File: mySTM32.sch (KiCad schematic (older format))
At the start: 114 parts, among them J1 conn1X2, J10 DB9_Female****, J11 USB_OTG, J12 conn2X16, J13 conn2X3, J14 Conn_02x02, J15 conn2X3, J16 conn1X2, J17 conn2X2, J18 JTAG, J19 Conn_02x17_Odd_Even, J2 USB_OTG, J20 Conn_02x22_Odd_Even, J21 conn2X9, J22 conn2X3, J23 Conn2x4, J3 conn2X3, J4 conn2X2, J5 conn2X2, J6 conn1X2, J7 Conn_01x02, J8 Conn2x4, J9 conn2X4, Q1 Q_NPN_BEC(S8050), Q2 Q_NPN_BEC, Q3 Q_NPN_BEC(S8050), SW1 KFT8.0, SW2 WAKUP, SW3 RESET, SW4 KE1, SW5 KEY2, U1 AT24C02, U2 W25Q16, U3 SD-Card, U4 SP3485, U5 SN65HVD230, U6 CH340G, U7 AMS1117, U8 SP3232, U9 STM32F103VET6, Y1 12MHz, Y2 32.768KHz, Y3 8MHz

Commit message: [power]
Signed-off-by: EasonLiang <liangyx25@163.com>
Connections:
- net +5V: no longer J15.2 (Pin_2), J15.4 (Pin_4), J15.6 (Pin_6)
- net 5V: now reaches C7.1, C9.1, SW1.2, SW1.5, U7.3 (VIN)
- net 5V: now also J15.2 (Pin_2), J15.4 (Pin_4), J15.6 (Pin_6)
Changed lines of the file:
@@
 $EndComp
 Connection ~ 6150 1200
-$Comp
-L power:+5V #PWR054
-U 1 1 62339161
-P 7100 1200
-F 0 "#PWR054" H 7100 1050 50  0001 C CNN
-F 1 "+5V" H 7115 1373 50  0000 C CNN
-F 2 "" H 7100 1200 50  0001 C CNN
-F 3 "" H 7100 1200 50  0001 C CNN
-	1    7100 1200
-	1    0    0    -1
-$EndComp
-Connection ~ 7100 1200
 Connection ~ 5650 1400
 Connection ~ 6600 1400
@@
 Wire Wire Line
 	1200 10350 1250 10350
+Text Label 2700 1100 0    50   ~ 0
+5V
+Text Label 7100 1200 0    50   ~ 0
+5V
 $EndSCHEMATC

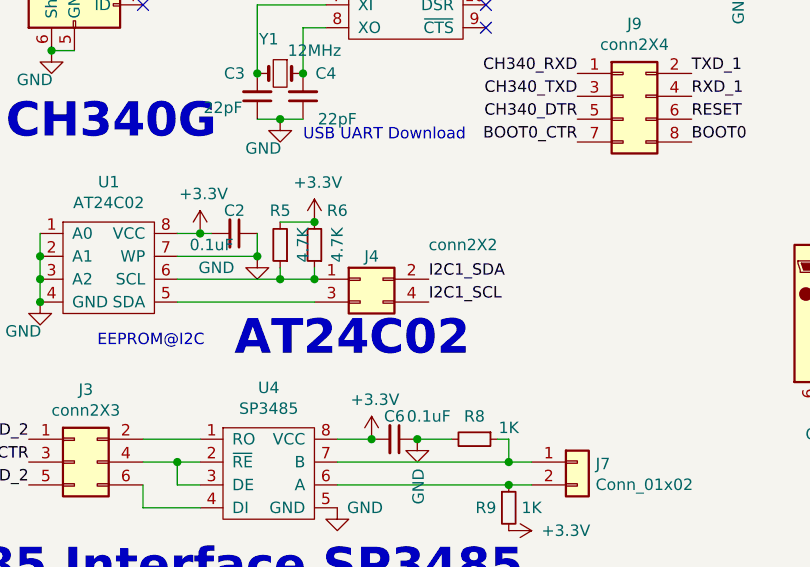
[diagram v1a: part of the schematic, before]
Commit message: [I2C EEPROM] [schematic validation on I2C ]
Signed-off-by: EasonLiang <liangyx25@163.com>
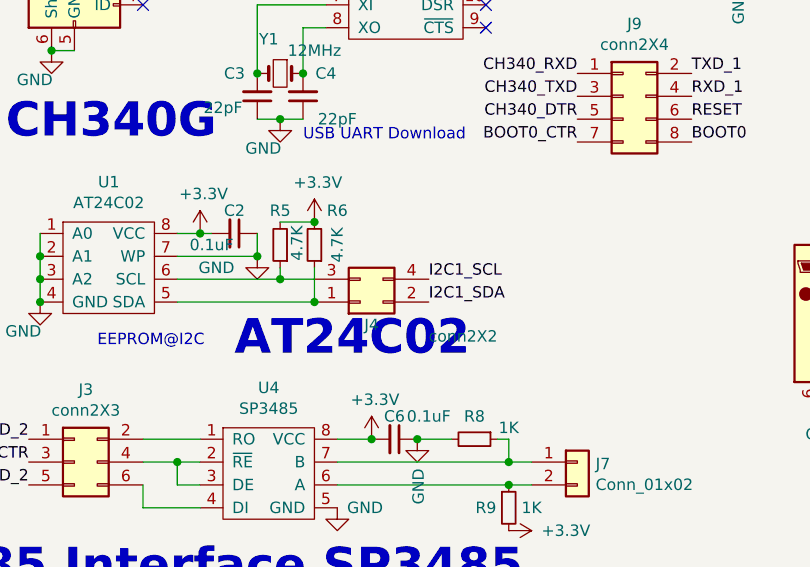
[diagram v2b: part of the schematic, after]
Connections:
- net at U1.5 (SDA): now also J4.1 (Pin_1), R6.1; no longer J4.3 (Pin_3)
- net at R5.1, U1.6 (SCL): now also J4.3 (Pin_3); no longer J4.1 (Pin_1), R6.1
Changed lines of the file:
@@
 Wire Wire Line
 	1650 3800 1700 3800
-$Comp
-L Connector_Generic:Conn_02x02_Odd_Even J4
-U 1 1 6115024C
-P 2350 4000
-F 0 "J4" H 2400 4100 50  0000 C CNN
-F 1 "conn2X2" H 2800 4150 50  0000 C CNN
-F 2 "mypcb:CON2X2" H 2350 4000 50  0001 C CNN
-F 3 "~" H 2350 4000 50  0001 C CNN
-	1    2350 4000
-	1    0    0    -1
-$EndComp
 Wire Wire Line
 	1550 4000 2000 4000
@@
 Text Label 10050 3200 2    50   ~ 0
 I2C1_SDA
+Text Label 2650 4000 0    50   ~ 0
+I2C1_SCL
 Text Label 2650 4100 0    50   ~ 0
-I2C1_SCL
-Text Label 2650 4000 0    50   ~ 0
 I2C1_SDA
 $Comp
@@
 P 2000 3850
 F 0 "R5" H 2000 3700 50  0000 C CNN
-F 1 "4.7K" V 1900 3850 50  0000 C CNN
+F 1 "4.7K" V 1926 3842 50  0000 C CNN
 F 2 "Resistor_SMD:R_0603_1608Metric" H 2000 3850 50  0001 C CNN
 F 3 "~" H 2000 3850 50  0001 C CNN
@@
 Wire Wire Line
 	2000 4000 2000 3950
-Wire Wire Line
-	2150 3950 2150 4000
 Wire Wire Line
 	2000 3750 2150 3750
@@
 Text Notes 8350 11000 0    151  ~ 30
 Buzzer
-Connection ~ 2150 4000
 Text Notes 10650 9100 0    151  ~ 30
 PWR_FLAG
@@
 Text Label 7100 1200 0    50   ~ 0
 5V
+$Comp
+L Connector_Generic:Conn_02x02_Odd_Even J4
+U 1 1 6115024C
+P 2350 4100
+F 0 "J4" H 2400 4200 50  0000 C CNN
+F 1 "conn2X2" H 2800 4250 50  0000 C CNN
+F 2 "mypcb:CON2X2" H 2350 4100 50  0001 C CNN
+F 3 "~" H 2350 4100 50  0001 C CNN
+	1    2350 4100
+	1    0    0    1
+$EndComp
+Connection ~ 2150 4100
+Wire Wire Line
+	2150 3950 2150 4100
 $EndSCHEMATC

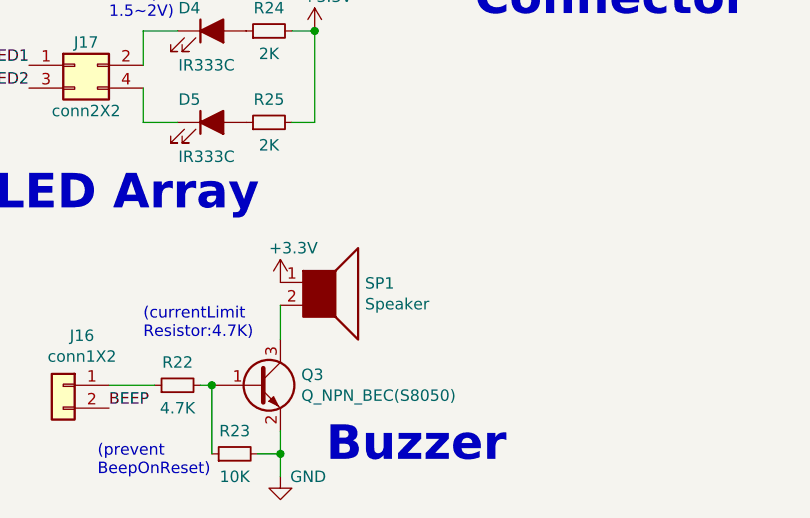
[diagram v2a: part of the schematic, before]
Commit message: [buzzer, lib] [layout] SD-Card
Signed-off-by: EasonLiang <liangyx25@163.com>
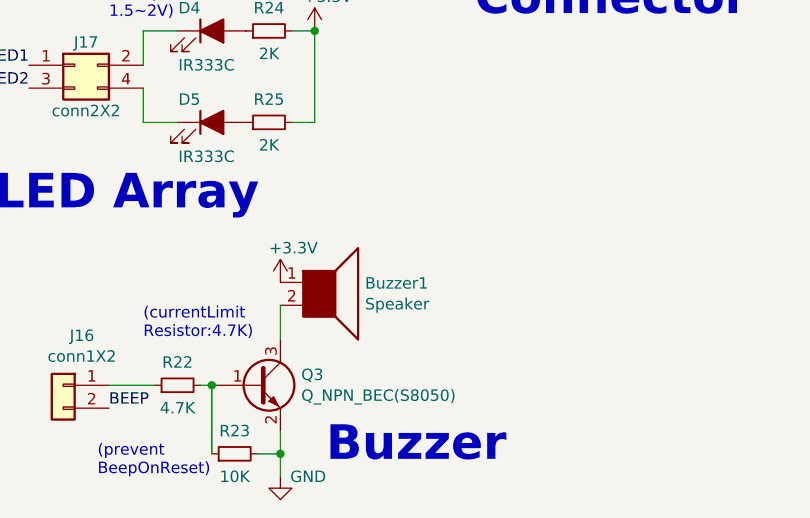
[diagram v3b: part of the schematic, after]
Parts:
- removed SP1: Speaker, mypcb:BEEP9X5.5, symbol mySTM32:Speaker
- added Buzzer1: Speaker, mypcb:BEEP9X5.5, symbol mySTM32:Speaker
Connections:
- net +3V3: now also Buzzer1.1
- net at Q3.3 (C): now also Buzzer1.2
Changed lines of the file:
@@
 LED Array
-$Comp
-L mySTM32:Speaker SP1
-U 1 1 6194AC61
-P 8350 10200
-F 0 "SP1" H 8520 10196 50  0000 L CNN
-F 1 "Speaker" H 8520 10105 50  0000 L CNN
-F 2 "mypcb:BEEP9X5.5" H 8350 10000 50  0001 C CNN
-F 3 "~" H 8340 10150 50  0001 C CNN
-	1    8350 10200
-	1    0    0    -1
-$EndComp
 $Comp
 L Device:Q_NPN_BEC Q3
@@
 Wire Wire Line
 	2150 3950 2150 4100
+$Comp
+L mySTM32:Speaker Buzzer1
+U 1 1 6156488F
+P 8350 10200
+F 0 "Buzzer1" H 8520 10196 50  0000 L CNN
+F 1 "Speaker" H 8520 10105 50  0000 L CNN
+F 2 "mypcb:BEEP9X5.5" H 8350 10000 50  0001 C CNN
+F 3 "~" H 8340 10150 50  0001 C CNN
+	1    8350 10200
+	1    0    0    -1
+$EndComp
 $EndSCHEMATC

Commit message: [IR Tx] [IR Rx]
Signed-off-by: EasonLiang <liangyx25@163.com>
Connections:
- net IE: now also J5.3 (Pin_3); no longer J5.1 (Pin_1)
- net IR: now also J5.1 (Pin_1); no longer J5.3 (Pin_3)
- net PB0: now also J5.2 (Pin_2); no longer J5.4 (Pin_4)
- net PB1: now also J5.4 (Pin_4); no longer J5.2 (Pin_2)
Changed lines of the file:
@@
 L Connector_Generic:Conn_02x02_Odd_Even J5
 U 1 1 612C9CBD
-P 2500 10500
-F 0 "J5" H 2550 10600 50  0000 C CNN
-F 1 "conn2X2" H 2550 10300 50  0000 C CNN
-F 2 "mypcb:CON2X2" H 2500 10500 50  0001 C CNN
-F 3 "~" H 2500 10500 50  0001 C CNN
-	1    2500 10500
-	1    0    0    -1
+P 2500 10600
+F 0 "J5" H 2550 10700 50  0000 C CNN
+F 1 "conn2X2" H 2550 10400 50  0000 C CNN
+F 2 "mypcb:CON2X2" H 2500 10600 50  0001 C CNN
+F 3 "~" H 2500 10600 50  0001 C CNN
+	1    2500 10600
+	1    0    0    1
 $EndComp
 Text Label 2300 10500 2    50   ~ 0
